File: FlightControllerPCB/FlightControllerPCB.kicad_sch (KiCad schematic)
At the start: 0 parts

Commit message: kicad structure
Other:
- added sheet Barometer (barometer.kicad_sch)
- added sheet IMU (imu.kicad_sch)
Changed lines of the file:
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@@
 	(generator_version "10.0")
 	(paper "A4")
+	(sheet
+		(at 40.64 38.1)
+		(size 50.8 25.4)
+		(exclude_from_sim no)
+		(in_bom yes)
+		(on_board yes)
+		(dnp no)
+		(fields_autoplaced yes)
+		(stroke
+			(width 0.1524)
+			(type solid)
+		)
+		(fill
+			(color 0 0 0 0)
+		)
+		(property "Sheetname" "Barometer"
+			(at 40.64 37.3884 0)
+			(show_name no)
+			(do_not_autoplace no)
+			(effects
+				(font
+					(size 1.27 1.27)
+					(thickness 0.254)
+					(bold yes)
+				)
+				(justify left bottom)
+			)
+		)
+		(property "Sheetfile" "barometer.kicad_sch"
+			(at 40.64 64.0846 0)
+			(hide yes)
+			(show_name no)
+			(do_not_autoplace no)
+			(effects
+				(font
+					(size 1.27 1.27)
+				)
+				(justify left top)
+			)
+		)
+		(instances
+			(project "FlightControllerPCB"
+				(path "/76f1a6d4-2c8f-4e0d-a089-f3ef3841ff54"
+					(page "2")
+				)
+			)
+		)
+	)
+	(sheet
+		(at 40.64 76.2)
+		(size 50.8 24.13)
+		(exclude_from_sim no)
+		(in_bom yes)
+		(on_board yes)
+		(dnp no)
+		(fields_autoplaced yes)
+		(stroke
+			(width 0.1524)
+			(type solid)
+		)
+		(fill
+			(color 0 0 0 0)
+		)
+		(property "Sheetname" "IMU"
+			(at 40.64 75.4884 0)
+			(show_name no)
+			(do_not_autoplace no)
+			(effects
+				(font
+					(size 1.27 1.27)
+					(thickness 0.254)
+					(bold yes)
+				)
+				(justify left bottom)
+			)
+		)
+		(property "Sheetfile" "imu.kicad_sch"
+			(at 40.64 100.9146 0)
+			(hide yes)
+			(show_name no)
+			(do_not_autoplace no)
+			(effects
+				(font
+					(size 1.27 1.27)
+				)
+				(justify left top)
+			)
+		)
+		(instances
+			(project "FlightControllerPCB"
+				(path "/76f1a6d4-2c8f-4e0d-a089-f3ef3841ff54"
+					(page "3")
+				)
+			)
+		)
+	)
 	(sheet_instances
 		(path "/"

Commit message: tester again
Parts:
- added U1: AD620, symbol Amplifier_Instrumentation:AD620
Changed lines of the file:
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@@
 	(generator_version "10.0")
 	(paper "A4")
+	(symbol
+		(lib_id "Amplifier_Instrumentation:AD620")
+		(at 132.08 68.58 0)
+		(unit 1)
+		(body_style 1)
+		(exclude_from_sim no)
+		(in_bom yes)
+		(on_board yes)
+		(in_pos_files yes)
+		(dnp no)
+		(fields_autoplaced yes)
+		(property "Reference" "U1"
+			(at 144.78 62.1598 0)
+			(show_name no)
+			(do_not_autoplace no)
+			(effects
+				(font
+					(size 1.27 1.27)
+				)
+			)
+		)
+		(property "Value" "AD620"
+			(at 144.78 64.6998 0)
+			(show_name no)
+			(do_not_autoplace no)
+			(effects
+				(font
+					(size 1.27 1.27)
+				)
+			)
+		)
+		(property "Footprint" ""
+			(at 132.08 68.58 0)
+			(hide yes)
+			(show_name no)
+			(do_not_autoplace no)
+			(effects
+				(font
+					(size 1.27 1.27)
+				)
+			)
+		)
+		(property "Datasheet" "https://www.analog.com/media/en/technical-documentation/data-sheets/AD620.pdf"
+			(at 132.08 68.58 0)
+			(hide yes)
+			(show_name no)
+			(do_not_autoplace no)
+			(effects
+				(font
+					(size 1.27 1.27)
+				)
+			)
+		)
+		(property "Description" "Low Cost, Low Power, Instrumentation Amplifier, DIP-8/SOIC-8"
+			(at 132.08 68.58 0)
+			(hide yes)
+			(show_name no)
+			(do_not_autoplace no)
+			(effects
+				(font
+					(size 1.27 1.27)
+				)
+			)
+		)
+		(pin "4"
+		)
+		(pin "7"
+		)
+		(pin "1"
+		)
+		(pin "6"
+		)
+		(pin "8"
+		)
+		(pin "2"
+		)
+		(pin "3"
+		)
+		(pin "5"
+		)
+		(instances
+			(project "FlightControllerPCB"
+				(path "/76f1a6d4-2c8f-4e0d-a089-f3ef3841ff54"
+					(reference "U1")
+					(unit 1)
+				)
+			)
+		)
+	)
 	(sheet
 		(at 40.64 38.1)

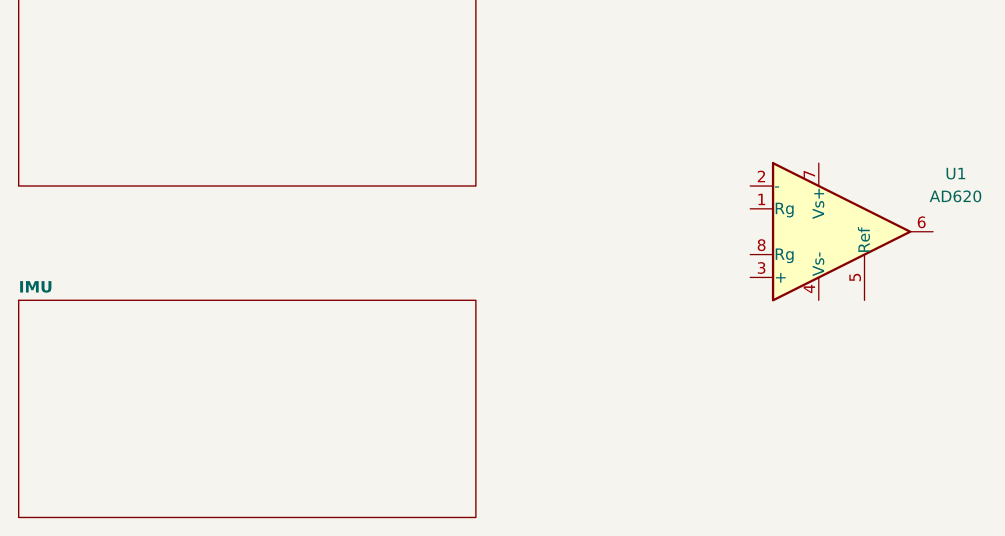
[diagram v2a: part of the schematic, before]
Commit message: IMU circuit
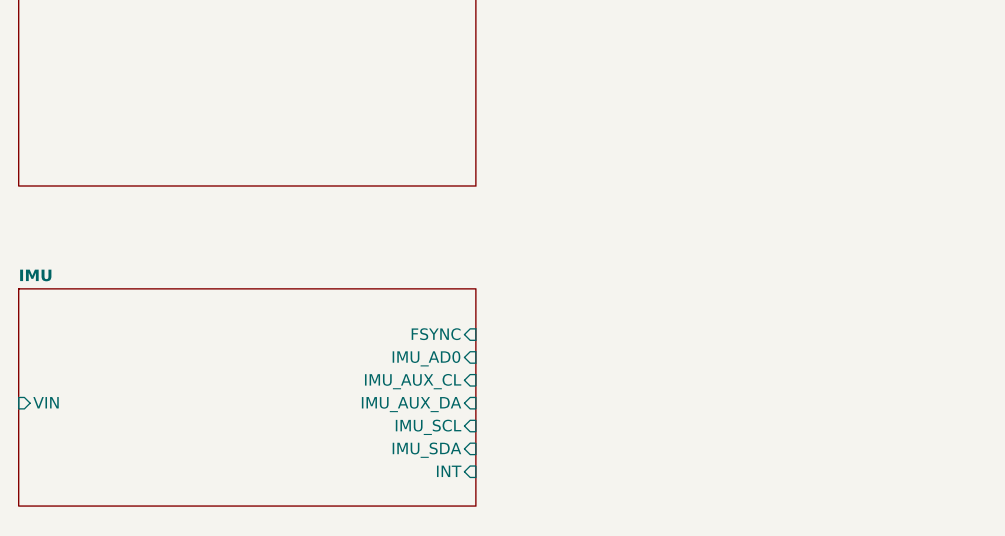
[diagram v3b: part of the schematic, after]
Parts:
- removed U1: AD620, symbol Amplifier_Instrumentation:AD620
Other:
- sheet IMU ports: added FSYNC, IMU_AD0, IMU_AUX_CL, IMU_AUX_DA, IMU_SCL, IMU_SDA, INT, VIN; removed none
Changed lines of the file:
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@@
 	(generator_version "10.0")
 	(paper "A4")
-	(symbol
-		(lib_id "Amplifier_Instrumentation:AD620")
-		(at 132.08 68.58 0)
-		(unit 1)
-		(body_style 1)
-		(exclude_from_sim no)
-		(in_bom yes)
-		(on_board yes)
-		(in_pos_files yes)
-		(dnp no)
-		(fields_autoplaced yes)
-		(property "Reference" "U1"
-			(at 144.78 62.1598 0)
-			(show_name no)
-			(do_not_autoplace no)
-			(effects
-				(font
-					(size 1.27 1.27)
-				)
-			)
-		)
-		(property "Value" "AD620"
-			(at 144.78 64.6998 0)
-			(show_name no)
-			(do_not_autoplace no)
-			(effects
-				(font
-					(size 1.27 1.27)
-				)
-			)
-		)
-		(property "Footprint" ""
-			(at 132.08 68.58 0)
-			(hide yes)
-			(show_name no)
-			(do_not_autoplace no)
-			(effects
-				(font
-					(size 1.27 1.27)
-				)
-			)
-		)
-		(property "Datasheet" "https://www.analog.com/media/en/technical-documentation/data-sheets/AD620.pdf"
-			(at 132.08 68.58 0)
-			(hide yes)
-			(show_name no)
-			(do_not_autoplace no)
-			(effects
-				(font
-					(size 1.27 1.27)
-				)
-			)
-		)
-		(property "Description" "Low Cost, Low Power, Instrumentation Amplifier, DIP-8/SOIC-8"
-			(at 132.08 68.58 0)
-			(hide yes)
-			(show_name no)
-			(do_not_autoplace no)
-			(effects
-				(font
-					(size 1.27 1.27)
-				)
-			)
-		)
-		(pin "4"
-		)
-		(pin "7"
-		)
-		(pin "1"
-		)
-		(pin "6"
-		)
-		(pin "8"
-		)
-		(pin "2"
-		)
-		(pin "3"
-		)
-		(pin "5"
-		)
-		(instances
-			(project "FlightControllerPCB"
-				(path "/76f1a6d4-2c8f-4e0d-a089-f3ef3841ff54"
-					(reference "U1")
-					(unit 1)
-				)
-			)
-		)
-	)
 	(sheet
 		(at 40.64 38.1)
@@
 	)
 	(sheet
-		(at 40.64 76.2)
+		(at 40.64 74.93)
 		(size 50.8 24.13)
 		(exclude_from_sim no)
@@
 		)
 		(property "Sheetname" "IMU"
-			(at 40.64 75.4884 0)
+			(at 40.64 74.2184 0)
 			(show_name no)
 			(do_not_autoplace no)
@@
 		)
 		(property "Sheetfile" "imu.kicad_sch"
-			(at 40.64 100.9146 0)
+			(at 40.64 99.6446 0)
 			(hide yes)
 			(show_name no)
@@
 			)
 		)
+		(pin "FSYNC" input
+			(at 91.44 80.01 0)
+			(effects
+				(font
+					(size 1.27 1.27)
+				)
+				(justify right)
+			)
+		)
+		(pin "IMU_AD0" input
+			(at 91.44 82.55 0)
+			(effects
+				(font
+					(size 1.27 1.27)
+				)
+				(justify right)
+			)
+		)
+		(pin "IMU_AUX_CL" input
+			(at 91.44 85.09 0)
+			(effects
+				(font
+					(size 1.27 1.27)
+				)
+				(justify right)
+			)
+		)
+		(pin "IMU_AUX_DA" input
+			(at 91.44 87.63 0)
+			(effects
+				(font
+					(size 1.27 1.27)
+				)
+				(justify right)
+			)
+		)
+		(pin "IMU_SCL" input
+			(at 91.44 90.17 0)
+			(effects
+				(font
+					(size 1.27 1.27)
+				)
+				(justify right)
+			)
+		)
+		(pin "IMU_SDA" input
+			(at 91.44 92.71 0)
+			(effects
+				(font
+					(size 1.27 1.27)
+				)
+				(justify right)
+			)
+		)
+		(pin "INT" input
+			(at 91.44 95.25 0)
+			(effects
+				(font
+					(size 1.27 1.27)
+				)
+				(justify right)
+			)
+		)
+		(pin "VIN" input
+			(at 40.64 87.63 180)
+			(effects
+				(font
+					(size 1.27 1.27)
+				)
+				(justify left)
+			)
+		)

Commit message: barometer schematic
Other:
- sheet Barometer ports: added BARO_INT, I2C1_SCK, I2C1_SDI; removed none
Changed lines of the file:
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@@
+			)
+		)
+		(pin "BARO_INT" input
+			(at 91.44 48.26 0)
+			(effects
+				(font
+					(size 1.27 1.27)
+				)
+				(justify right)
+			)
+		)
+		(pin "I2C1_SCK" input
+			(at 91.44 50.8 0)
+			(effects
+				(font
+					(size 1.27 1.27)
+				)
+				(justify right)
+			)
+		)
+		(pin "I2C1_SDI" input
+			(at 91.44 53.34 0)
+			(effects
+				(font
+					(size 1.27 1.27)
+				)
+				(justify right)
 			)
 		)

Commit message: some edits
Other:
- added sheet Magnometer (Mag.kicad_sch)
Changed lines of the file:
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@@
+		)
+	)
+	(sheet
+		(at 40.64 107.95)
+		(size 50.8 25.4)
+		(exclude_from_sim no)
+		(in_bom yes)
+		(on_board yes)
+		(dnp no)
+		(fields_autoplaced yes)
+		(stroke
+			(width 0.1524)
+			(type solid)
+		)
+		(fill
+			(color 0 0 0 0)
+		)
+		(property "Sheetname" "Magnometer"
+			(at 40.64 107.2384 0)
+			(show_name no)
+			(do_not_autoplace no)
+			(effects
+				(font
+					(size 1.27 1.27)
+				)
+				(justify left bottom)
+			)
+		)
+		(property "Sheetfile" "Mag.kicad_sch"
+			(at 40.64 133.9346 0)
+			(show_name no)
+			(do_not_autoplace no)
+			(effects
+				(font
+					(size 1.27 1.27)
+				)
+				(justify left top)
+			)
+		)
+		(instances
+			(project "FlightControllerPCB"
+				(path "/76f1a6d4-2c8f-4e0d-a089-f3ef3841ff54"
+					(page "4")
+				)
+			)
 		)
 	)

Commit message: Hella sheets
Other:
- added sheet MCU (MCU.kicad_sch)
- added sheet USB+POWER (power.kicad_sch)
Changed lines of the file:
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@@
 	(paper "A4")
 	(sheet
-		(at 40.64 38.1)
-		(size 50.8 25.4)
+		(at 247.65 20.32)
+		(size 21.59 83.82)
+		(exclude_from_sim no)
+		(in_bom yes)
+		(on_board yes)
+		(dnp no)
+		(fields_autoplaced yes)
+		(stroke
+			(width 0.1524)
+			(type solid)
+		)
+		(fill
+			(color 0 0 0 0)
+		)
+		(property "Sheetname" "USB+POWER"
+			(at 247.65 19.6084 0)
+			(show_name no)
+			(do_not_autoplace no)
+			(effects
+				(font
+					(size 1.27 1.27)
+				)
+				(justify left bottom)
+			)
+		)
+		(property "Sheetfile" "power.kicad_sch"
+			(at 247.65 104.7246 0)
+			(hide yes)
+			(show_name no)
+			(do_not_autoplace no)
+			(effects
+				(font
+					(size 1.27 1.27)
+				)
+				(justify left top)
+			)
+		)
+		(instances
+			(project "FlightControllerPCB"
+				(path "/76f1a6d4-2c8f-4e0d-a089-f3ef3841ff54"
+					(page "6")
+				)
+			)
+		)
+	)
+	(sheet
+		(at 17.78 17.78)
+		(size 21.59 25.4)
 		(exclude_from_sim no)
 		(in_bom yes)
@@
 		)
 		(property "Sheetname" "Barometer"
-			(at 40.64 37.3884 0)
+			(at 17.78 17.0684 0)
 			(show_name no)
 			(do_not_autoplace no)
@@
 		)
 		(property "Sheetfile" "barometer.kicad_sch"
-			(at 40.64 64.0846 0)
+			(at 17.78 43.7646 0)
 			(hide yes)
 			(show_name no)
@@
 		)
 		(pin "BARO_INT" input
-			(at 91.44 48.26 0)
+			(at 39.37 27.94 0)
 			(effects
 				(font
@@
 		)
 		(pin "I2C1_SCK" input
-			(at 91.44 50.8 0)
+			(at 39.37 30.48 0)
 			(effects
 				(font
@@
 		)
 		(pin "I2C1_SDI" input
-			(at 91.44 53.34 0)
+			(at 39.37 33.02 0)
 			(effects
 				(font
@@
 	)
 	(sheet
-		(at 40.64 74.93)
-		(size 50.8 24.13)
+		(at 80.01 16.51)
+		(size 127 20.32)
+		(exclude_from_sim no)
+		(in_bom yes)
+		(on_board yes)
+		(dnp no)
+		(fields_autoplaced yes)
+		(stroke
+			(width 0.1524)
+			(type solid)
+		)
+		(fill
+			(color 0 0 0 0)
+		)
+		(property "Sheetname" "MCU"
+			(at 80.01 15.7984 0)
+			(show_name no)
+			(do_not_autoplace no)
+			(effects
+				(font
+					(size 1.27 1.27)
+				)
+				(justify left bottom)
+			)
+		)
+		(property "Sheetfile" "MCU.kicad_sch"
+			(at 80.01 37.4146 0)
+			(hide yes)
+			(show_name no)
+			(do_not_autoplace no)
+			(effects
+				(font
+					(size 1.27 1.27)
+				)
+				(justify left top)
+			)
+		)
+		(instances
+			(project "FlightControllerPCB"
+				(path "/76f1a6d4-2c8f-4e0d-a089-f3ef3841ff54"
+					(page "5")
+				)
+			)
+		)
+	)
+	(sheet
+		(at 17.78 54.61)
+		(size 21.59 24.13)
 		(exclude_from_sim no)
 		(in_bom yes)
@@
 		)
 		(property "Sheetname" "IMU"
-			(at 40.64 74.2184 0)
+			(at 17.78 53.8984 0)
 			(show_name no)
 			(do_not_autoplace no)
@@
 		)
 		(property "Sheetfile" "imu.kicad_sch"
-			(at 40.64 99.6446 0)
+			(at 17.78 79.3246 0)
 			(hide yes)
 			(show_name no)
@@
 		)
 		(pin "FSYNC" input
-			(at 91.44 80.01 0)
+			(at 39.37 59.69 0)
 			(effects
 				(font
@@
 		)
 		(pin "IMU_AD0" input
-			(at 91.44 82.55 0)
+			(at 39.37 62.23 0)
 			(effects
 				(font
@@
 		)
 		(pin "IMU_AUX_CL" input
-			(at 91.44 85.09 0)
+			(at 39.37 64.77 0)
 			(effects
 				(font
@@
 		)
 		(pin "IMU_AUX_DA" input
-			(at 91.44 87.63 0)
+			(at 39.37 67.31 0)
 			(effects
 				(font
@@
 		)
 		(pin "IMU_SCL" input
-			(at 91.44 90.17 0)
+			(at 39.37 69.85 0)
 			(effects
 				(font
@@
 		)
 		(pin "IMU_SDA" input
-			(at 91.44 92.71 0)
+			(at 39.37 72.39 0)
 			(effects
 				(font
@@
 		)
 		(pin "INT" input
-			(at 91.44 95.25 0)
+			(at 39.37 74.93 0)
 			(effects
 				(font
@@
 		)
 		(pin "VIN" input
-			(at 40.64 87.63 180)
+			(at 17.78 67.31 180)
 			(effects
 				(font
@@
 	)
 	(sheet
-		(at 40.64 107.95)
-		(size 50.8 25.4)
+		(at 17.78 87.63)
+		(size 21.59 25.4)
 		(exclude_from_sim no)
 		(in_bom yes)
@@
 		)
 		(property "Sheetname" "Magnometer"
-			(at 40.64 107.2384 0)
+			(at 17.78 86.9184 0)
 			(show_name no)
 			(do_not_autoplace no)
@@
 		)
 		(property "Sheetfile" "Mag.kicad_sch"
-			(at 40.64 133.9346 0)
-			(show_name no)
-			(do_not_autoplace no)
+			(at 17.78 113.6146 0)
+			(hide yes)
+			(show_name no)
+			(do_not_autoplace no)

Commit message: Early MCU Setup
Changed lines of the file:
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@@
 				(font
 					(size 1.27 1.27)
+					(thickness 0.254)
+					(bold yes)
 				)
 				(justify left bottom)
@@
 				(font
 					(size 1.27 1.27)
+					(thickness 0.254)
+					(bold yes)
 				)
 				(justify left bottom)
@@
 				(font
 					(size 1.27 1.27)
-				)
-				(justify left bottom)
+					(thickness 0.254)
+					(bold yes)
+				)
+				(justify left bottom)

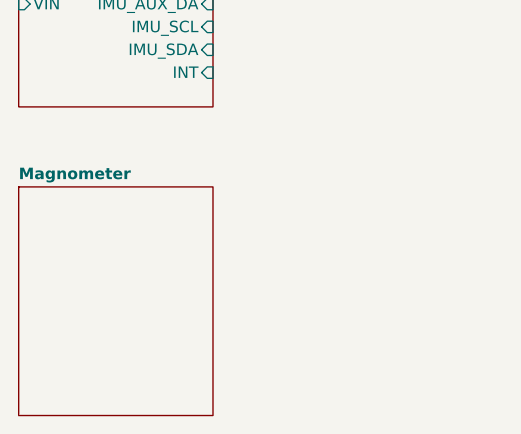
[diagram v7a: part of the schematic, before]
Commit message: remove mag
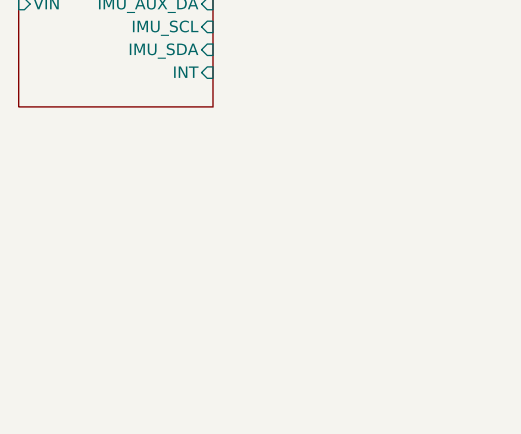
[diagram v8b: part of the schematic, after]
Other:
- removed sheet Magnometer
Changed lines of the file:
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@@
-		)
-	)
-	(sheet
-		(at 17.78 87.63)
-		(size 21.59 25.4)
-		(exclude_from_sim no)
-		(in_bom yes)
-		(on_board yes)
-		(dnp no)
-		(fields_autoplaced yes)
-		(stroke
-			(width 0.1524)
-			(type solid)
-		)
-		(fill
-			(color 0 0 0 0)
-		)
-		(property "Sheetname" "Magnometer"
-			(at 17.78 86.9184 0)
-			(show_name no)
-			(do_not_autoplace no)
-			(effects
-				(font
-					(size 1.27 1.27)
-					(thickness 0.254)
-					(bold yes)
-				)
-				(justify left bottom)
-			)
-		)
-		(property "Sheetfile" "Mag.kicad_sch"
-			(at 17.78 113.6146 0)
-			(hide yes)
-			(show_name no)
-			(do_not_autoplace no)
-			(effects
-				(font
-					(size 1.27 1.27)
-				)
-				(justify left top)
-			)
-		)
-		(instances
-			(project "FlightControllerPCB"
-				(path "/76f1a6d4-2c8f-4e0d-a089-f3ef3841ff54"
-					(page "4")
-				)
-			)
 		)
 	)
